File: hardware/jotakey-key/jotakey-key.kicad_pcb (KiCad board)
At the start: 2 copper layers, 0 parts

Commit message: hardware: bring the schematic's footprints onto the board
All 27 footprints, staged next to the (still empty) board area with
their nets: the 24 standard parts and the three from the project
library (USB-A edge contacts, OPTIGA USON-10, logo touch electrode).
Done with KiCad's own Update PCB from Schematic, since Konnect cannot
place custom-shape pads. No outline, placement or routing yet.

Co-Authored-By: Claude Opus 5.5 <noreply@anthropic.com>
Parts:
- added C1: 1uF, Capacitor_SMD:C_0402_1005Metric, F.Cu at (101.4, 74.5)
- added C10: 10nF C0G, Capacitor_SMD:C_0402_1005Metric, F.Cu at (107.1, 78.4)
- added C2: 1uF, Capacitor_SMD:C_0402_1005Metric, F.Cu at (101.4, 76.5)
- added C3: 4.7uF, Capacitor_SMD:C_0603_1608Metric, F.Cu at (109.3, 83.3)
- added C4: 100nF, Capacitor_SMD:C_0402_1005Metric, F.Cu at (101.4, 78.4)
- added C5: 100nF, Capacitor_SMD:C_0402_1005Metric, F.Cu at (104.3, 74.5)
- added C6: 100nF, Capacitor_SMD:C_0402_1005Metric, F.Cu at (104.3, 76.5)
- added C7: 1uF, Capacitor_SMD:C_0402_1005Metric, F.Cu at (104.3, 78.4)
- added C8: 100nF, Capacitor_SMD:C_0402_1005Metric, F.Cu at (107.1, 74.5)
- added C9: 100nF, Capacitor_SMD:C_0402_1005Metric, F.Cu at (107.1, 76.5)
- added D1: LED red, LED_SMD:LED_0603_1608Metric, F.Cu at (109.3, 80.7)
- added E1: TouchPad, jotakey:TouchPad_D10mm, F.Cu at (207.5, 95.4)
- added J1: USB_A_PCB_Edge, jotakey:USB_A_PCB_Edge_2.0mm, F.Cu at (194.6, 89.8)
- added R1: 1k, Resistor_SMD:R_0402_1005Metric, F.Cu at (98.5, 74.5)
- added R2: 1k, Resistor_SMD:R_0402_1005Metric, F.Cu at (98.5, 76.5)
- added R3: 4.7k, Resistor_SMD:R_0402_1005Metric, F.Cu at (98.5, 78.5)
- added R4: 4.7k, Resistor_SMD:R_0402_1005Metric, F.Cu at (98.5, 80.5)
- added R5: 10k, Resistor_SMD:R_0402_1005Metric, F.Cu at (98.5, 82.5)
- added TP1: SWDIO, TestPoint:TestPoint_Pad_D1.0mm, F.Cu at (95.5, 75.0)
- added TP2: SWCLK, TestPoint:TestPoint_Pad_D1.0mm, F.Cu at (95.5, 78.1)
- added TP3: NRST, TestPoint:TestPoint_Pad_D1.0mm, F.Cu at (95.5, 81.1)
- added TP4: 3V3, TestPoint:TestPoint_Pad_D1.0mm, F.Cu at (95.5, 84.2)
- added TP5: GND, TestPoint:TestPoint_Pad_D1.0mm, F.Cu at (95.5, 87.2)
- added U1: STM32L432KCU6, Package_DFN_QFN:QFN-32-1EP_5x5mm_P0.5mm_EP3.45x3.45mm, F.Cu at (103.6, 83.1)
- added U2: SLS32AIA010MH, jotakey:Infineon_PG-USON-10-2_3x3mm_P0.5mm_EP1.7x2.5mm, F.Cu at (204.1, 104.1)
- added U3: XC6206P332MR, Package_TO_SOT_SMD:SOT-23-3, F.Cu at (102.5, 88.9)
- added U4: USBLC6-2SC6, Package_TO_SOT_SMD:SOT-23-6, F.Cu at (107.7, 89.1)

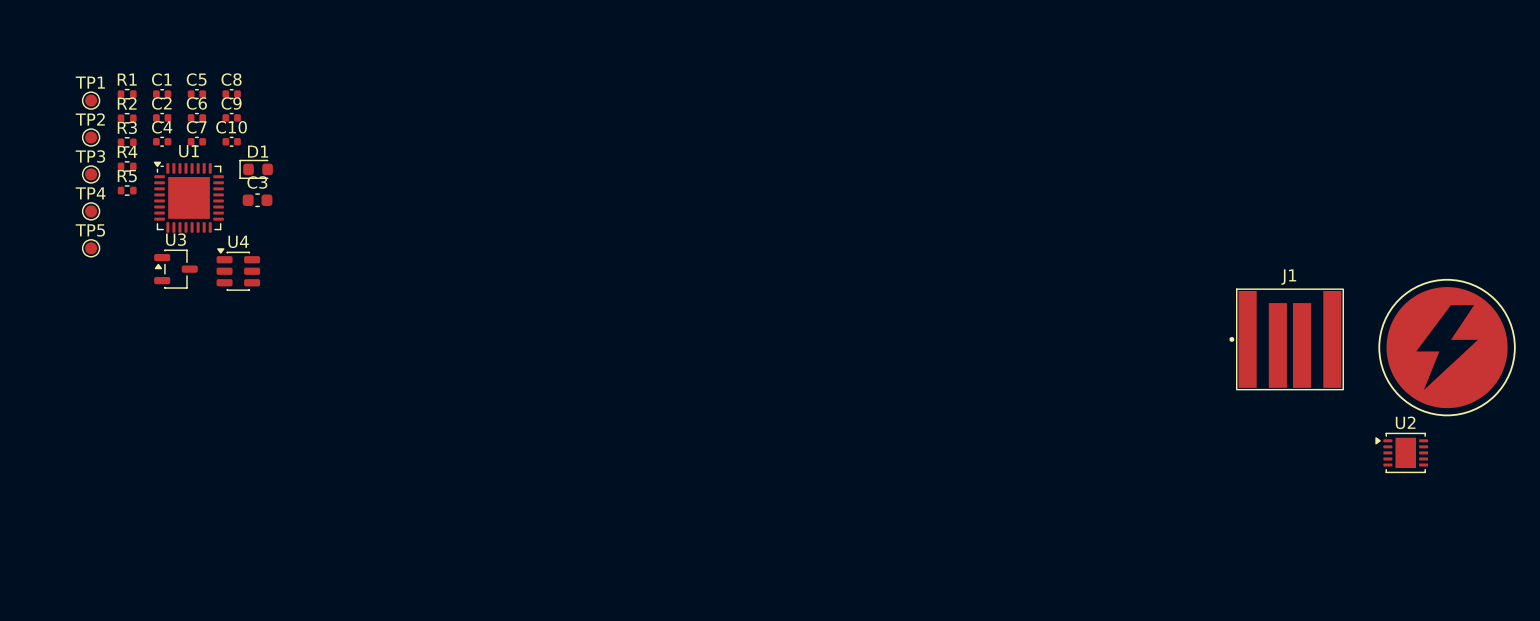
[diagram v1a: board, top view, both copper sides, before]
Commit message: hardware: place the parts and draw the board outline
tools/layout.py draws the outline (USB-A tongue, body with a rounded end)
and places every footprint through KiCad's IPC API. The touch electrode
is concentric with the rounded end; the decoupling, NRST and touch parts
sit next to the MCU pins they serve. No keyring hole.

The touch electrode footprint loses its silkscreen ring and puts its
reference on F.Fab: no ink over the electrode or its logo.

DRC: no courtyard, clearance or short violations; only unrouted nets and
silkscreen text warnings remain.

Co-Authored-By: Claude Opus 5.5 <noreply@anthropic.com>
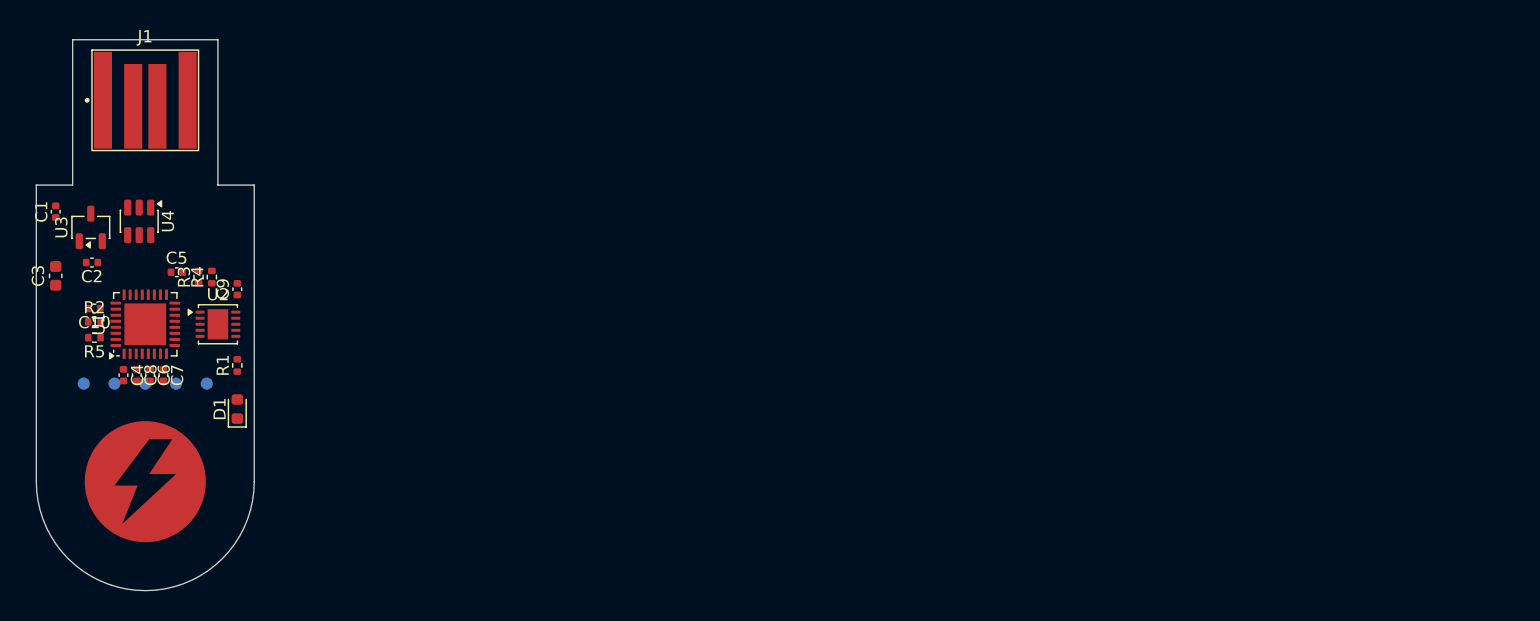
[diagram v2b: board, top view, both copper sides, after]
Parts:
- TP1, TP2, TP3, TP4, TP5: moved to B.Cu
- moved E1 108.1 mm to (100.0, 106.5)
- moved U2 98.7 mm to (106.0, 93.5)
- moved J1 96.6 mm to (100.0, 70.0)
- moved C8 24.5 mm to (99.3, 97.7), turned to -90 degrees
- moved R1 24.2 mm to (107.6, 96.9), turned to 90 degrees
- moved TP1 23.4 mm to (94.9, 98.4)
- moved C6 21.6 mm to (100.4, 97.7), turned to -90 degrees
- moved TP2 20.4 mm to (97.5, 98.4)
- moved D1 19.9 mm to (107.6, 100.5), turned to 90 degrees
- moved C4 19.5 mm to (98.2, 97.7), turned to -90 degrees
- moved C7 19.5 mm to (101.5, 97.7), turned to -90 degrees
- moved TP3 17.8 mm to (100.0, 98.4)
- moved C10 17.8 mm to (95.8, 92.2), turned to 180 degrees
- moved C3 17.8 mm to (92.6, 89.5), turned to 90 degrees
- moved R2 17.0 mm to (95.8, 93.3)
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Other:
- board outline added: 18 x 45.5 mm

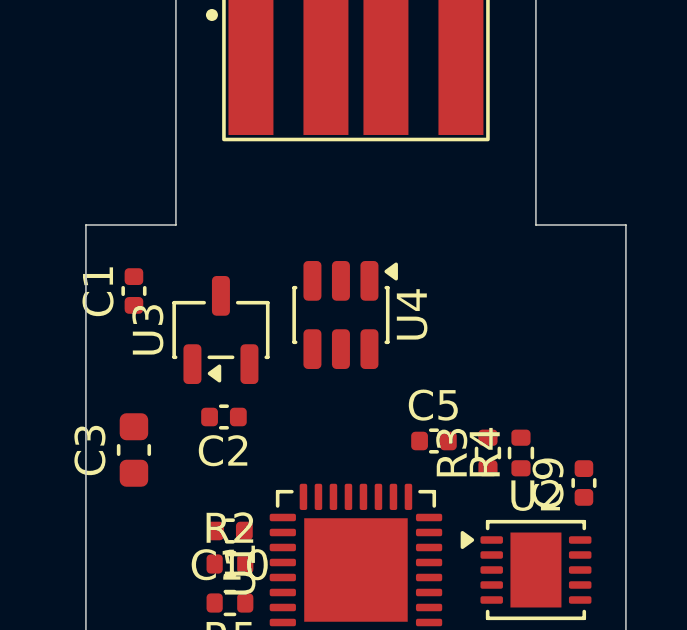
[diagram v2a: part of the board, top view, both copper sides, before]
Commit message: hardware: name the touch electrode net, centre U4 and swap its channels
The touch electrode's net gets a label, TOUCH_ELECTRODE, instead of
KiCad's generated Net-(E1-~).

U4 (USBLC6-2SC6) moves onto the board's centre line. Its two channels
are identical, so D- now passes through pins 3/4 and D+ through pins 1/6.
This puts the one unavoidable D+/D- crossing between U4 and the MCU,
where there is room for vias, instead of on the USB-A tongue.

Co-Authored-By: Claude Opus 5.5 <noreply@anthropic.com>
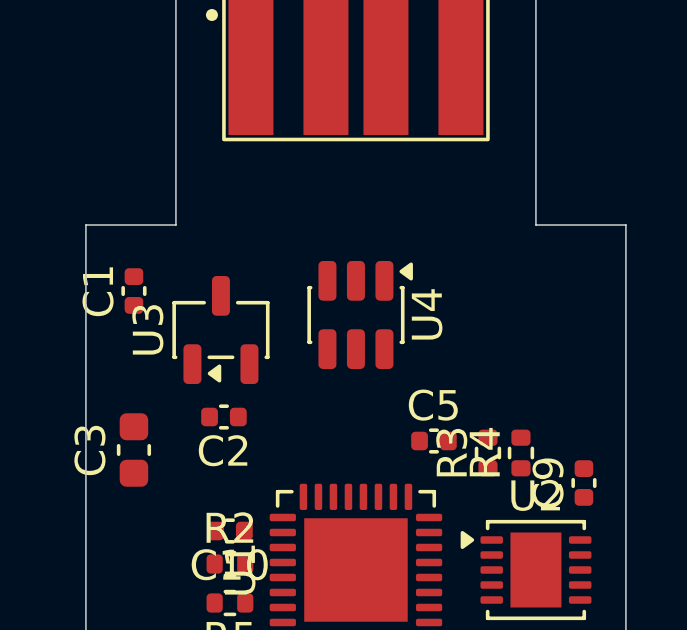
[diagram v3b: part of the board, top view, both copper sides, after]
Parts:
- moved U4 0.50 mm to (100.0, 85.0)
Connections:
- net Net-(E1-~) renamed /TOUCH_ELECTRODE
- U4 pad 1: /USB_CONN_DM -> /USB_CONN_DP
- U4 pad 3: /USB_CONN_DP -> /USB_CONN_DM
- U4 pad 4: /USB_DP -> /USB_DM
- U4 pad 6: /USB_DM -> /USB_DP
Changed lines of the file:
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@@
 	(footprint "Package_TO_SOT_SMD:SOT-23-6"
 		(layer "F.Cu")
-		(at 99.5 85 -90)
+		(at 100 85 -90)
 		(descr "SOT, 6 Pin (JEDEC MO-178 Var AB https://www.jedec.org/document_search?search_api_views_fulltext=MO-178)")
 		(tags "SOT TO_SOT_SMD")
@@
 			(layers "F.Cu" "F.Mask" "F.Paste")
 			(roundrect_rratio 0.25)
-			(net "/USB_CONN_DM")
+			(net "/USB_CONN_DP")
 			(pinfunction "I/O1_1")
 			(pintype "passive")
@@
 			(layers "F.Cu" "F.Mask" "F.Paste")
 			(roundrect_rratio 0.25)
-			(net "/USB_CONN_DP")
+			(net "/USB_CONN_DM")
 			(pinfunction "I/O2_3")
 			(pintype "passive")
@@
 			(layers "F.Cu" "F.Mask" "F.Paste")
 			(roundrect_rratio 0.25)
-			(net "/USB_DP")
+			(net "/USB_DM")
 			(pinfunction "I/O2_4")
 			(pintype "passive")
@@
 			(layers "F.Cu" "F.Mask" "F.Paste")
 			(roundrect_rratio 0.25)
-			(net "/USB_DM")
+			(net "/USB_DP")
 			(pinfunction "I/O1_6")
 			(pintype "passive")
@@
 		)
 		(fp_text user "${REFERENCE}"
-			(at 0 0 360)
+			(at 0 0 0)
 			(layer "F.Fab")
 			(effects
@@
 			(layers "F.Cu" "F.Mask" "F.Paste")
 			(roundrect_rratio 0.25)
-			(net "Net-(E1-~)")
+			(net "/TOUCH_ELECTRODE")
 			(pinfunction "~_1")
 			(pintype "passive")
@@
 		(tags "capacitor")
 		(property "Reference" "C6"
-			(at 0 -1.16 -90)
+			(at 0 -1.16 270)
 			(layer "F.SilkS")
 			(effects
@@
 		)
 		(property "Value" "100nF"
-			(at 0 1.16 -90)
+			(at 0 1.16 270)
 			(layer "F.Fab")
 			(effects
@@
 		)
 		(property "Datasheet" "~"
-			(at 0 0 -90)
+			(at 0 0 270)
 			(layer "F.Fab")
 			(hide yes)
@@
 		)
 		(property "Description" "Unpolarized capacitor"
-			(at 0 0 -90)
+			(at 0 0 270)
 			(layer "F.Fab")
 			(hide yes)
@@
 		)
 		(property "KiLib_Generator" "SMD_2terminal_chip_molded"
-			(at 0 0 -90)
+			(at 0 0 270)
 			(layer "F.SilkS")
 			(hide yes)
@@
 		)
 		(property "LCSC" "C1525"
-			(at 0 0 -90)
+			(at 0 0 270)
 			(unlocked yes)
 			(layer "F.Fab")
@@
 		)
 		(property "MPN" "CL05B104KO5NNNC"
-			(at 0 0 -90)
+			(at 0 0 270)
 			(unlocked yes)
 			(layer "F.Fab")
@@
 		(tags "capacitor")
 		(property "Reference" "C7"
-			(at 0 -1.16 -90)
+			(at 0 -1.16 270)
 			(layer "F.SilkS")
 			(effects
@@
 		)
 		(property "Value" "1uF"
-			(at 0 1.16 -90)
+			(at 0 1.16 270)
 			(layer "F.Fab")
 			(effects
@@
 		)
 		(property "Datasheet" "~"
-			(at 0 0 -90)
+			(at 0 0 270)
 			(layer "F.Fab")
 			(hide yes)
@@
 		)
 		(property "Description" "Unpolarized capacitor"
-			(at 0 0 -90)
+			(at 0 0 270)
 			(layer "F.Fab")
 			(hide yes)
@@
 		)
 		(property "KiLib_Generator" "SMD_2terminal_chip_molded"
-			(at 0 0 -90)
+			(at 0 0 270)
 			(layer "F.SilkS")
 			(hide yes)
@@
 		)
 		(property "LCSC" "C52923"
-			(at 0 0 -90)
+			(at 0 0 270)
 			(unlocked yes)
 			(layer "F.Fab")
@@
 		)
 		(property "MPN" "CL05A105KA5NQNC"
-			(at 0 0 -90)
+			(at 0 0 270)
 			(unlocked yes)
 			(layer "F.Fab")
@@
 		(tags "capacitor")
 		(property "Reference" "C8"
-			(at 0 -1.16 -90)
+			(at 0 -1.16 270)
 			(layer "F.SilkS")
 			(effects
@@
 		)
 		(property "Value" "100nF"
-			(at 0 1.16 -90)
+			(at 0 1.16 270)
 			(layer "F.Fab")
 			(effects
@@
 		)
 		(property "Datasheet" "~"
-			(at 0 0 -90)
+			(at 0 0 270)
 			(layer "F.Fab")
 			(hide yes)
@@
 		)
 		(property "Description" "Unpolarized capacitor"
-			(at 0 0 -90)
+			(at 0 0 270)
 			(layer "F.Fab")
 			(hide yes)
@@
 		)
 		(property "KiLib_Generator" "SMD_2terminal_chip_molded"
-			(at 0 0 -90)
+			(at 0 0 270)
 			(layer "F.SilkS")
 			(hide yes)
@@
 		)
 		(property "LCSC" "C1525"
-			(at 0 0 -90)
+			(at 0 0 270)
 			(unlocked yes)
 			(layer "F.Fab")
@@
 		)
 		(property "MPN" "CL05B104KO5NNNC"
-			(at 0 0 -90)
+			(at 0 0 270)
 			(unlocked yes)
 			(layer "F.Fab")
@@
 			(size 0.4 0.4)
 			(layers "F.Cu")
-			(net "Net-(E1-~)")
+			(net "/TOUCH_ELECTRODE")
 			(pinfunction "~_1")
 			(pintype "passive")
@@
 		(tags "capacitor")
 		(property "Reference" "C4"
-			(at 0 -1.16 -90)
+			(at 0 -1.16 270)
 			(layer "F.SilkS")
 			(effects
@@
 		)
 		(property "Value" "100nF"
-			(at 0 1.16 -90)
+			(at 0 1.16 270)
 			(layer "F.Fab")
 			(effects
@@
 		)
 		(property "Datasheet" "~"
-			(at 0 0 -90)
+			(at 0 0 270)
 			(layer "F.Fab")
 			(hide yes)
@@
 		)
 		(property "Description" "Unpolarized capacitor"
-			(at 0 0 -90)
+			(at 0 0 270)
 			(layer "F.Fab")
 			(hide yes)
@@
 		)
 		(property "KiLib_Generator" "SMD_2terminal_chip_molded"
-			(at 0 0 -90)
+			(at 0 0 270)
 			(layer "F.SilkS")
 			(hide yes)
@@
 		)
 		(property "LCSC" "C1525"
-			(at 0 0 -90)
+			(at 0 0 270)
 			(unlocked yes)
 			(layer "F.Fab")
@@
 		)
 		(property "MPN" "CL05B104KO5NNNC"
-			(at 0 0 -90)
+			(at 0 0 270)
 			(unlocked yes)
 			(layer "F.Fab")

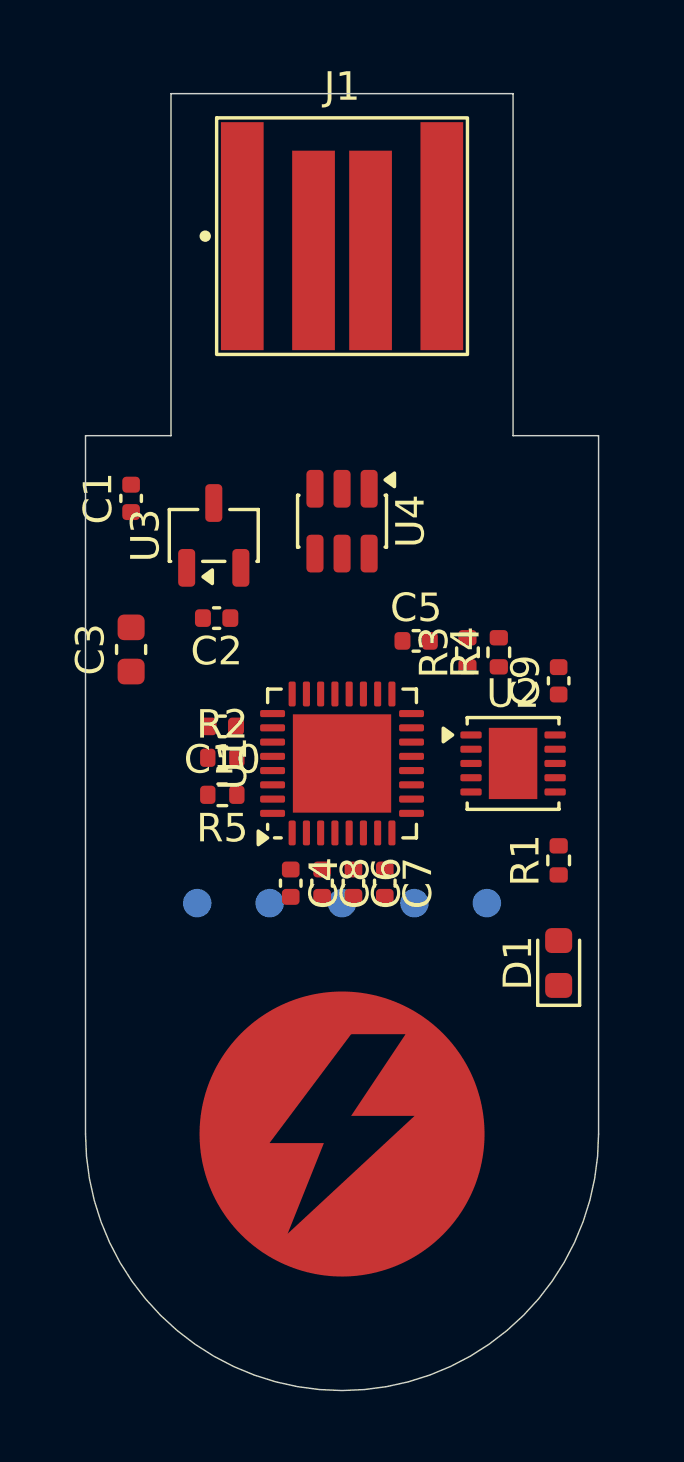
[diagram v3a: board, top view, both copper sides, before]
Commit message: hardware: route the board
tools/route.py routes the board from the placement: keep-outs (nothing
under the touch electrode, a 1 mm ground gap around it, no vias or
bottom copper on the USB-A tongue, 0.5 mm from the board edge), the
critical nets by hand (USB with its one D+/D- crossing, VBUS, the touch
electrode trace, the capacitors and NRST under the MCU), Freerouting 2.5
for the rest, then GND pours on both layers. DRC: no errors and no
unconnected items.

To make the board routable:
- the LED moves from PA8 (pin 18) to PA3 (pin 9), off the crowded top
  row of the MCU and next to the LED;
- the OPTIGA reset moves from PB0 (pin 14) to PA5 (pin 11);
- the OPTIGA moves to the top-right corner, rotated so SCL, RST and VCC
  face the MCU; its pull-ups and decoupling move with it;
- R1 turns round so the LED track does not wrap around it.
HARDWARE.md records the new pins.

tools/silk.py moves reference designators to the fab layers (they cannot
sit beside 0402 parts on this board without covering pads) and marks a
2 x 10 mm block on the bottom silkscreen for JLCPCB's serial number.

Co-Authored-By: Claude Opus 5.5 <noreply@anthropic.com>
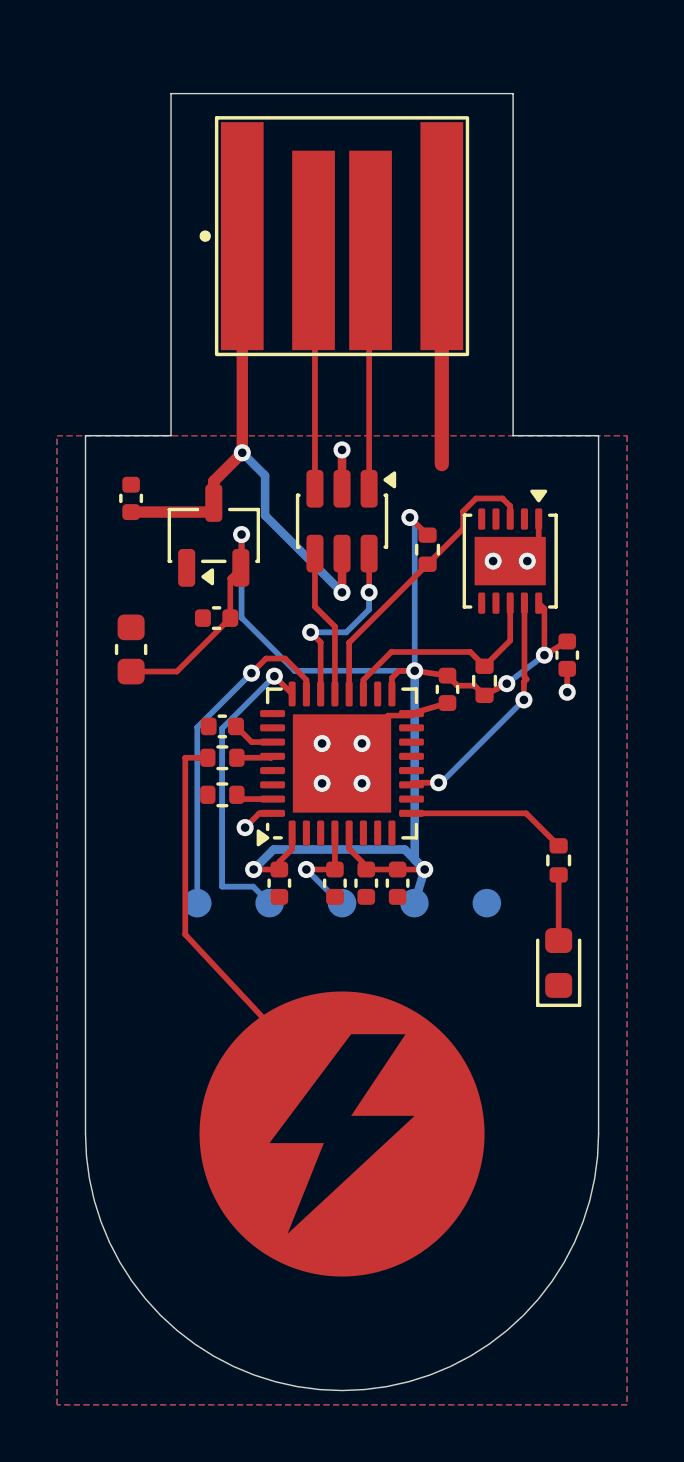
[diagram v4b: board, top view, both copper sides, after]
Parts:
- moved U2 7.10 mm to (105.9, 86.4), turned to -90 degrees
- moved R3 3.86 mm to (103.0, 86.0), turned to -90 degrees
- moved C5 2.02 mm to (103.7, 90.9), turned to -90 degrees
- moved R4 1.12 mm to (105.0, 90.6)
- moved C9 0.95 mm to (107.9, 89.7), turned to -90 degrees
- moved C7 0.45 mm to (102.0, 97.7)
- moved C8 0.45 mm to (99.8, 97.7)
- moved C6 0.45 mm to (100.8, 97.7)
- moved C4 0.40 mm to (97.8, 97.7)
- turned R1 to -90 degrees
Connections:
- U1 pad 11: unconnected-(U1-PA5-Pad11) -> /SE_RST
- U1 pad 14: /SE_RST -> unconnected-(U1-PB0-Pad14)
- U1 pad 18: /LED -> unconnected-(U1-PA8-Pad18)
- U1 pad 9: unconnected-(U1-PA3-Pad9) -> /LED
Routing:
- net +3V3: track 0.00 -> 53.9 mm, vias 0 -> 7
- net VBUS: track 0.00 -> 20.7 mm, vias 0 -> 2
- net /TOUCH_ELECTRODE: track 0.00 -> 15.7 mm
- net /SWDIO: track 0.00 -> 11.8 mm, vias 0 -> 1
- net /SWCLK: track 0.00 -> 10.9 mm, vias 0 -> 1
- net GND: track 0.00 -> 10.9 mm, vias 0 -> 9
- net /I2C_SDA: track 0.00 -> 10.5 mm
- net /SE_RST: track 0.00 -> 8.64 mm, vias 0 -> 2
- net /USB_CONN_DP: track 0.00 -> 8.38 mm
- net /USB_CONN_DM: track 0.00 -> 8.38 mm
- net /I2C_SCL: track 0.00 -> 7.95 mm
- net /USB_DP: track 0.00 -> 6.65 mm, vias 0 -> 2
- net /LED: track 0.00 -> 5.63 mm
- net /USB_DM: track 0.00 -> 5.21 mm
- net /NRST: track 0.00 -> 4.04 mm, vias 0 -> 1
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- added copper zone on B.Cu, net GND
- added copper zone on F.Cu, net GND
